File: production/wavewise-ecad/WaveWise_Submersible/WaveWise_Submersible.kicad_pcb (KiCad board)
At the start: 4 copper layers, 136.8 x 50.8 mm, 91 parts, among them J1 SMA_CONNECTOR, J10 Screw_Terminal_01x03, J11 Screw_Terminal_01x03, J2 SMA_CONNECTOR, J3 Screw_Terminal_01x04, J4 Screw_Terminal_01x03, J5 SMA_CONNECTOR, J6 USB_B_Micro, J7 Screw_Terminal_01x03, J8 Screw_Terminal_01x03, J9 Screw_Terminal_01x02, M1 MNMOS, M2 MNMOS, U1 ATMEGA328PB-ANR, U2 KP234XTMA1, U3 SI8600AC-B-ISR, U4 EZO_pH_Circuit, U5 SI8600AC-B-ISR, U6 EZO_Conductivity_Circuit, U7 TLV2462CP, U8 FT232RL-REEL, Y1 AS-16.000-20-SMD-TR

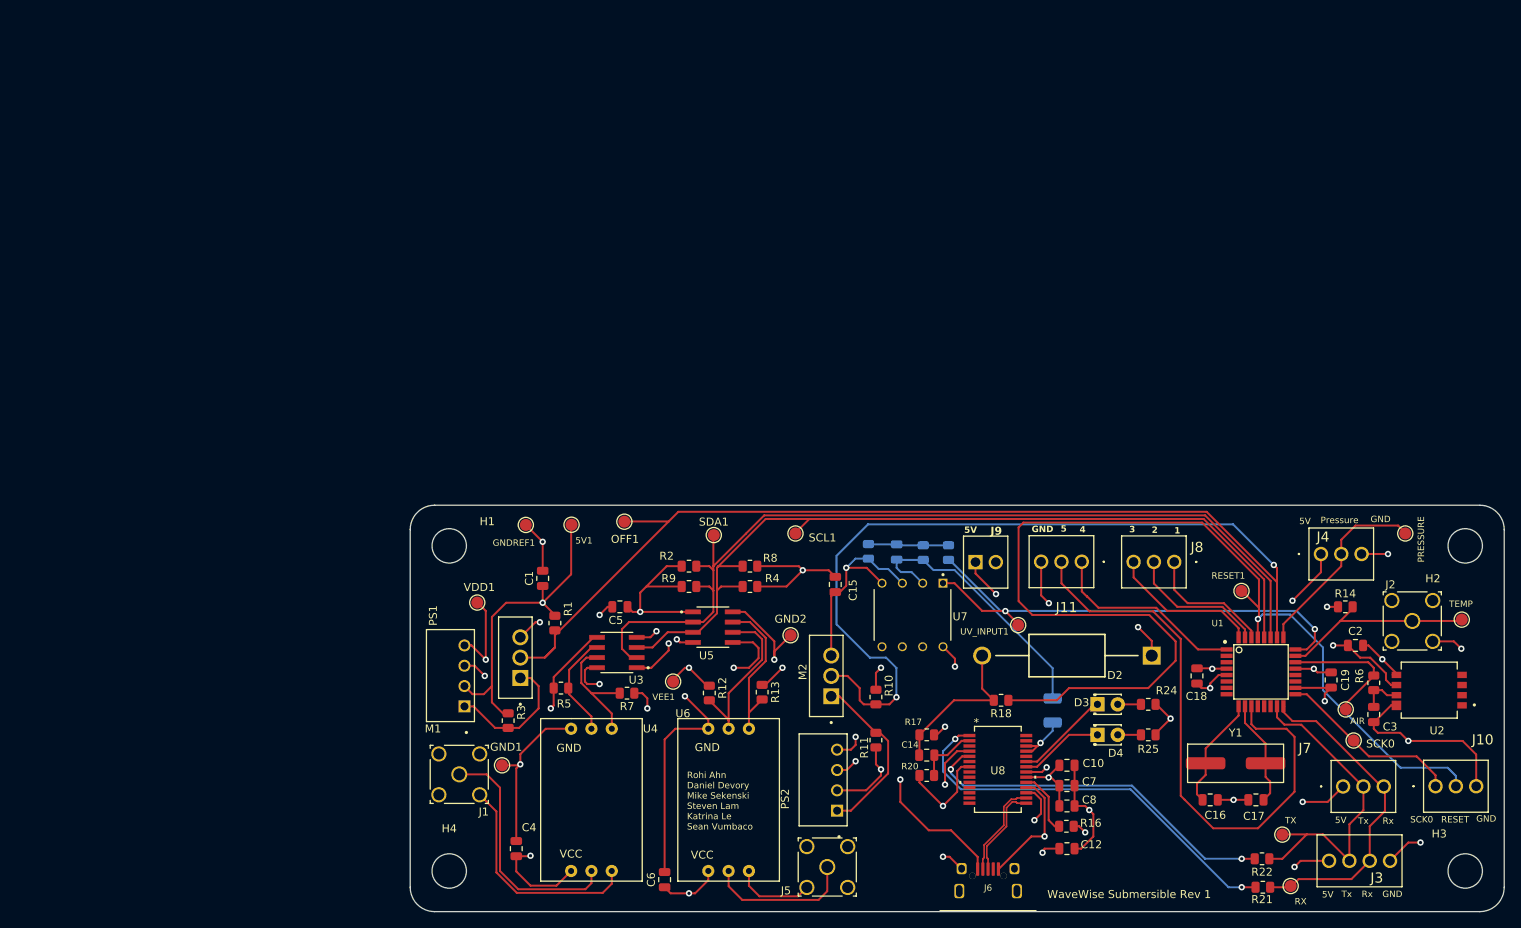
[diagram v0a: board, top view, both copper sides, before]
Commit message: layout first draft, added general/connector footprint
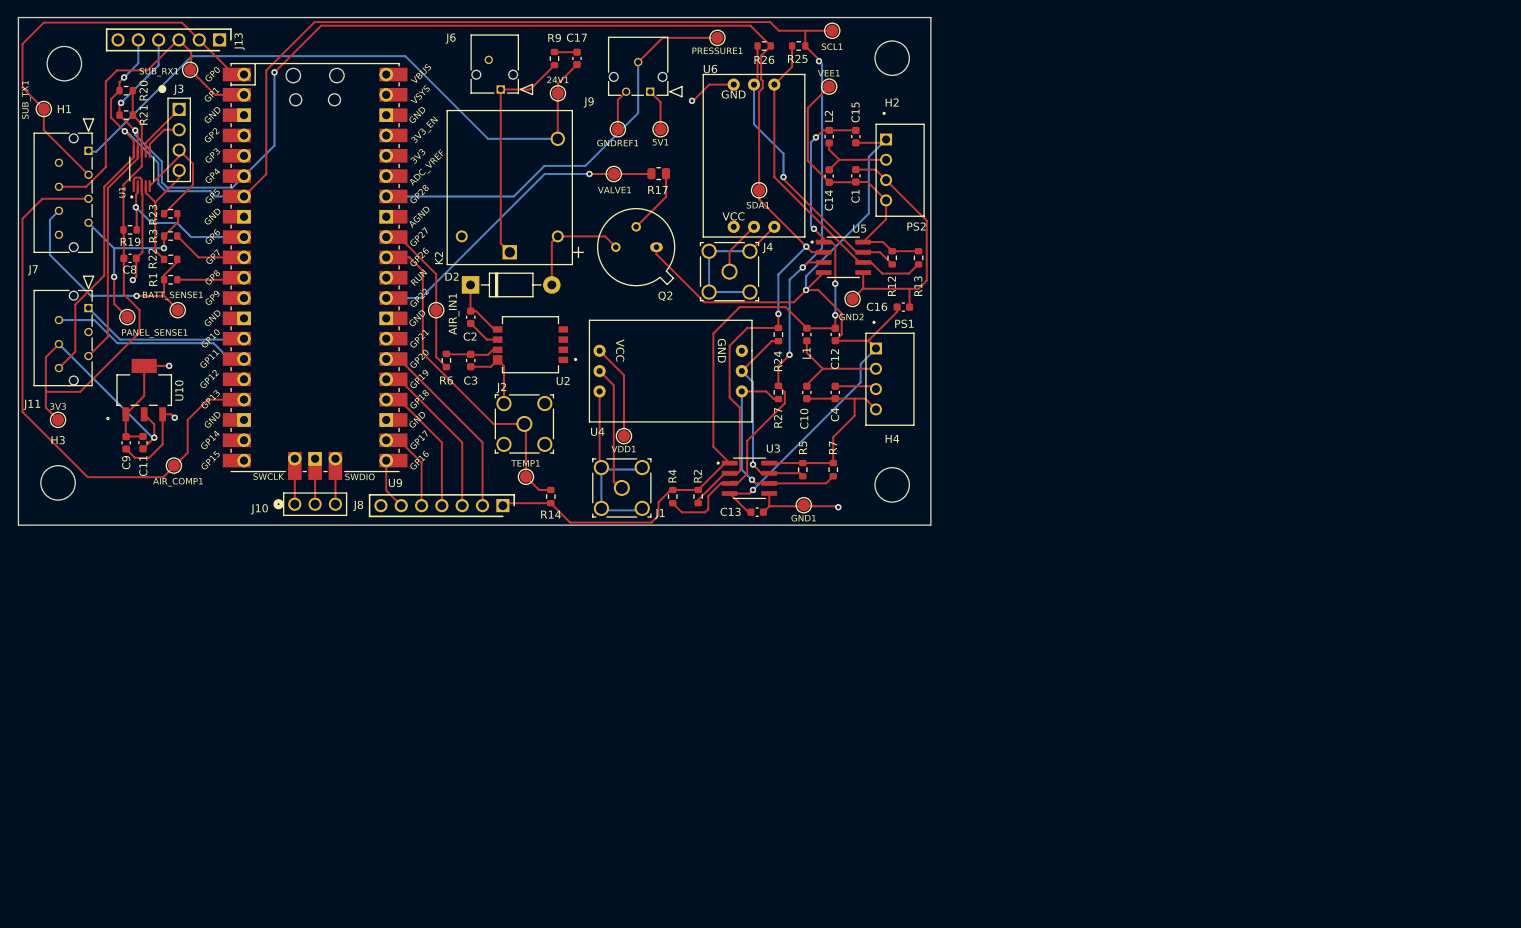
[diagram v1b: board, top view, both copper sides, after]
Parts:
- removed AIR, OFF1, PRESSURE, RESET1, RX, SCK0, TEMP, TX, UV_INPUT1: TestPoint, TestPoint:TestPoint_Pad_D1.5mm
- removed C18, C19, C7: 100n/10V, Capacitor_SMD:C_0805_2012Metric
- removed C5, C6: 1u/10V, Capacitor_SMD:C_0805_2012Metric
- removed D1: D_Photo, WW_Checked:GUVA-S12SD
- removed D3, D4: LED_S, LED_THT:LED_D1.8mm_W3.3mm_H2.4mm
- removed J5: SMA_CONNECTOR, Unchecked:SMA_Jack
- removed M1, M2: MNMOS, Unchecked:nMOS_ThroughHole
- removed R10, R11: 1M, Resistor_SMD:R_0805_2012Metric
- removed R15: 1k, Resistor_SMD:R_0805_2012Metric
- removed R16: 10k, Resistor_SMD:R_0805_2012Metric
- removed R18: 0, Resistor_SMD:R_0805_2012Metric
- removed R8: 10K, Resistor_SMD:R_0805_2012Metric
- removed U7: TLV2462CP, Unchecked:TLV2462CP
- removed U8: FT232RL-REEL, Unchecked:IC28_SSOP-28_FTD
- removed Y1: AS-16.000-20-SMD-TR, WW_Checked:WW_Oscillator
- added 24V1: TestPoint, TestPoint:TestPoint_Pad_D1.5mm, F.Cu at (105.0, 34.9)
- added 3V3: TestPoint, TestPoint:TestPoint_Pad_D1.5mm, F.Cu at (42.5, 75.7)
- added AIR_COMP1: TestPoint, TestPoint:TestPoint_Pad_D1.5mm, F.Cu at (57.0, 81.4)
- added AIR_IN1: TestPoint, TestPoint:TestPoint_Pad_D1.5mm, F.Cu at (89.8, 62.0)
- added BATT_SENSE1: TestPoint, TestPoint:TestPoint_Pad_D1.5mm, F.Cu at (57.5, 62.0)
- added C11: 22u, Capacitor_SMD:C_0603_1608Metric, F.Cu at (53.2, 78.5)
- added C9: 10u, Capacitor_SMD:C_0603_1608Metric, F.Cu at (51.1, 78.6)
- added J13: Conn_01x06_Pin, Connector:61300611121, F.Cu at (62.7, 28.2)
- added K2: AWHSH105D00G, Relay_SMD:AWHSH105D00G, F.Cu at (99.0, 54.8)
- added L1: 22u, Inductor_SMD:L_0603_1608Metric, F.Cu at (136.1, 65.0)
- added L2: 22u, Inductor_SMD:L_0603_1608Metric, F.Cu at (138.9, 40.3)
- added PANEL_SENSE1: TestPoint, TestPoint:TestPoint_Pad_D1.5mm, F.Cu at (51.2, 62.8)
- added PRESSURE1: TestPoint, TestPoint:TestPoint_Pad_D1.5mm, F.Cu at (125.0, 27.9)
- added Q2: 2N2219, Package_TO_SOT_THT:TO-39-3, F.Cu at (117.3, 54.1)
- added R26: 0, Resistor_SMD:R_0603_1608Metric, F.Cu at (130.8, 29.0)
- added R27: 0, Resistor_SMD:R_0603_1608Metric, F.Cu at (132.6, 72.3)
- added SUB_RX1: TestPoint, TestPoint:TestPoint_Pad_D1.5mm, F.Cu at (59.1, 31.9)
- added SUB_TX1: TestPoint, TestPoint:TestPoint_Pad_D1.5mm, F.Cu at (40.8, 36.8)
- added TEMP1: TestPoint, TestPoint:TestPoint_Pad_D1.5mm, F.Cu at (101.0, 82.8)
- added U10: AZ1117CH-3.3TRG1, Package_TO_SOT_SMD:SOT-223_DIO, F.Cu at (53.3, 72.0)
- added U9: Raspberry Pi Pico, MCU_RaspberryPi_and_Boards:RPi_Pico_SMD_TH, F.Cu at (74.7, 56.7)
- added VALVE1: TestPoint, TestPoint:TestPoint_Pad_D1.5mm, F.Cu at (112.0, 45.0)
- C1, C4: value 1u/10V -> 1u; footprint Capacitor_SMD:C_0805_2012Metric -> Capacitor_SMD:C_0603_1608Metric
- C10: value 4.7u/10V -> 330p; footprint Capacitor_SMD:C_0805_2012Metric -> Capacitor_SMD:C_0603_1608Metric
- C12: value 100n/10V -> 6.8u; footprint Capacitor_SMD:C_0805_2012Metric -> Capacitor_SMD:C_0603_1608Metric
- C13: value 0.1uF/10V -> 330p; footprint Capacitor_SMD:C_0805_2012Metric -> Capacitor_SMD:C_0603_1608Metric; moved to F.Cu
- C14: value 100n/10V -> 330p; footprint Capacitor_SMD:C_0805_2012Metric -> Capacitor_SMD:C_0603_1608Metric
- C15: value 0.1uF/10V -> 6.8u; footprint Capacitor_SMD:C_0805_2012Metric -> Capacitor_SMD:C_0603_1608Metric
- C16: value 22pF/10V -> 330p; footprint Capacitor_SMD:C_0805_2012Metric -> Capacitor_SMD:C_0603_1608Metric
- C17: value 22pF/10V -> 1u; footprint Capacitor_SMD:C_0805_2012Metric -> Capacitor_SMD:C_0603_1608Metric
- C2, C3: value 100nF/10V -> 100nF; footprint Capacitor_SMD:C_0805_2012Metric -> Capacitor_SMD:C_0603_1608Metric
- C8: value 100n/10V -> 0.1u; footprint Capacitor_SMD:C_0805_2012Metric -> Capacitor_SMD:C_0603_1608Metric
- D2: value 1N5822 -> 1N5817; footprint Unchecked:1N5822 -> Diode_THT:D_DO-41_SOD81_P10.16mm_Horizontal
- J1, J2: footprint Unchecked:SMA_Jack -> Connector:SMA_Jack
- J10: value Screw_Terminal_01x03 -> Conn_01x03_Pin; footprint WW_Checked:ScrewTerminal_01x03_2.54mm -> Connector:61300311121
- J11: value Screw_Terminal_01x03 -> 5031750600; footprint WW_Checked:ScrewTerminal_01x03_2.54mm -> Connector:5031750600
- J3: value Screw_Terminal_01x04 -> Conn_01x04_Pin; footprint WW_Checked:ScrewTerminal_01x04_2.54mm -> Connector:61300411121
- J4: value Screw_Terminal_01x03 -> SMA_CONNECTOR; footprint WW_Checked:ScrewTerminal_01x03_2.54mm -> Connector:SMA_Jack
- J6: value USB_B_Micro -> 5031750200; footprint WW_Checked:MicroUSB_Mount -> Connector:5031750200
- J7: value Screw_Terminal_01x03 -> 5031750800; footprint WW_Checked:ScrewTerminal_01x03_2.54mm -> Connector:5031750800
- J8: value Screw_Terminal_01x03 -> Conn_01x07_Pin; footprint WW_Checked:ScrewTerminal_01x03_2.54mm -> Connector:61300711121
- J9: value Screw_Terminal_01x02 -> 5031750300; footprint WW_Checked:ScrewTerminal_01x02_2.54mm -> Connector:5031750300
- PS1, PS2: footprint WW_Checked:RFM-0505S -> Converter_DCDC:RFM-0505S
- R1, R3: value 1M -> 0; footprint Resistor_SMD:R_0805_2012Metric -> Resistor_SMD:R_0603_1608Metric
- R12, R13, R14, R2, R4, R5, R6, R7: footprint Resistor_SMD:R_0805_2012Metric -> Resistor_SMD:R_0603_1608Metric
- R17: value 10k -> 5k
- R19: value 1M -> 10k; footprint Resistor_SMD:R_0805_2012Metric -> Resistor_SMD:R_0603_1608Metric; moved to F.Cu
- R20, R21: value 1k -> 10k; footprint Resistor_SMD:R_0805_2012Metric -> Resistor_SMD:R_0603_1608Metric
- R22: value 1k -> 0; footprint Resistor_SMD:R_0805_2012Metric -> Resistor_SMD:R_0603_1608Metric
- R23: value 3.3k -> 0; footprint Resistor_SMD:R_0805_2012Metric -> Resistor_SMD:R_0603_1608Metric; moved to F.Cu
- R24, R25: value R -> 0; footprint Resistor_SMD:R_0805_2012Metric -> Resistor_SMD:R_0603_1608Metric
- R9: value 10K -> 50; footprint Resistor_SMD:R_0805_2012Metric -> Resistor_SMD:R_0603_1608Metric
- U1: value ATMEGA328PB-ANR -> ADS1115IDGSR; footprint Unchecked:ATMEGA328PB-ANR -> Converter_ACDC:SOP50P490X110-10N
- U2: footprint Unchecked:XDCR_KP234XTMA1 -> Sensor_Pressure:XDCR_KP234XTMA1
- U3, U5: footprint Unchecked:SOIC127P600X175-8N -> Package_SO:SI8600AC-B-ISR
- U4: footprint WW_Checked:EZO_pH_Circuit -> Sensor:EZO_pH_Circuit
- U6: footprint WW_Checked:EZO_Conductivity_Circuit -> Sensor:EZO_Conductivity_Circuit
- moved H3 182.5 mm to (42.5, 83.6)
- moved J7 175.8 mm to (46.4, 42.1), turned to -90 degrees
- moved R21 171.8 mm to (51.1, 37.6), turned to 180 degrees
- moved J3 171.7 mm to (57.7, 36.9), turned to -90 degrees
- moved R22 155.6 mm to (56.6, 55.6), turned to 0 degrees
- moved U1 153.4 mm to (53.0, 44.3), turned to 90 degrees
- moved J10 146.9 mm to (72.1, 86.2)
- moved C8 135.6 mm to (51.5, 55.5), turned to 180 degrees
- moved R20 131.7 mm to (51.1, 34.5), turned to 180 degrees
- moved J11 128.1 mm to (46.4, 61.7), turned to -90 degrees
- moved C17 125.7 mm to (107.4, 30.5), turned to -90 degrees
- moved R6 122.7 mm to (91.1, 68.3), turned to -90 degrees
- moved C3 121.2 mm to (94.1, 68.3)
- moved U2 120.4 mm to (101.6, 66.3)
- moved C2 118.0 mm to (94.1, 62.9), turned to -90 degrees
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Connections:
- C1 pad 1: +5V -> VEE
- C1 pad 2: GNDREF -> GND2
- C10 pad 1: +5V -> VDD
- C10 pad 2: GNDREF -> Net-(PS1-+VIN)
- C12 pad 1: +3V3 -> +5V
- C13 pad 1: Net-(D1-K) -> GND1
- C13 pad 2: Net-(C13-Pad2) -> GNDREF
- C14 pad 1: Net-(C14-Pad1) -> VEE
- C14 pad 2: Net-(U8-DTR#) -> Net-(PS2-+VIN)
- C16 pad 1: Net-(U1-PD5) -> GND2
- C17 pad 1: Net-(U1-PD6) -> Net-(C17-Pad1)
- C17 pad 2: GNDREF -> +24V
- C8 pad 1: +5V -> GNDREF
- C8 pad 2: GNDREF -> +3V3
- J1 pad 2: (no net) -> Net-(U4-PGND)
- J1 pad 3: (no net) -> Net-(U4-PGND)
- J1 pad 5: (no net) -> Net-(U4-PGND)
- J10 pad 1: SCK0 -> SWCLK
- J10 pad 2: RESET -> GND
- J10 pad 3: GNDREF -> SWDIO
- J11 pad 1: EXTGPIO4 -> SYNC
- J11 pad 2: EXTGPIO5 -> READY/INT
- J2 pad 2: (no net) -> GNDREF
- J2 pad 3: (no net) -> GNDREF
- J2 pad 5: (no net) -> GNDREF
- J3 pad 1: +5V -> /ADC3
- J3 pad 2: SUB_TX -> /ADC2
- J3 pad 3: SUB_RX -> /ADC1
- J3 pad 4: GNDREF -> /ADC0
- J4 pad 1: +5V -> Net-(U6-PRB)
- J4 pad 2: PRESSURE_INPUT -> Net-(U6-PGND)
- J4 pad 3: GNDREF -> Net-(U6-PGND)
- J6 pad 1: +5V -> Net-(J6-Pad1)
- J6 pad 2: /USB- -> GNDREF
- J7 pad 1: +5V -> +24V
- J7 pad 2: SUB_TX -> +5V
- J7 pad 3: SUB_RX -> SUB_TX
- J8 pad 1: EXTGPIO1 -> +5V
- J8 pad 2: EXTGPIO2 -> EXTGPIO1
- J8 pad 3: EXTGPIO3 -> EXTGPIO2
- J9 pad 2: unconnected-(J9-Pin_2-Pad2) -> PRESSURE_INPUT
- PS1 pad 1: Net-(M1-D) -> GNDREF
- PS1 pad 2: +5V -> Net-(PS1-+VIN)
- PS2 pad 1: Net-(M2-D) -> GNDREF
- PS2 pad 2: +5V -> Net-(PS2-+VIN)
- R1 pad 1: +5V -> BATTERY_SENSE
- R1 pad 2: OFF -> Net-(U9-GPIO8)
- R17 pad 1: Net-(C14-Pad1) -> VALVE_OUT
- R17 pad 2: +5V -> Net-(Q2-B)
- R19 pad 1: Net-(D1-K) -> +3V3
- R19 pad 2: Net-(C13-Pad2) -> ADC_RDY
- R20 pad 1: GNDREF -> +3V3
- R20 pad 2: Net-(U8-DTR#) -> SCL
- R21 pad 1: Net-(U8-TXD) -> +3V3
- R21 pad 2: SUB_RX -> SDA
- R22 pad 1: SUB_TX -> /ADC0
- R22 pad 2: Net-(U8-RXD) -> BATTERY_SENSE
- R23 pad 1: UV_INPUT -> /ADC1
- R23 pad 2: Net-(C13-Pad2) -> PANEL_SENSE
- R24 pad 1: Net-(D3-A) -> SDA
- R24 pad 2: +5V -> Net-(U3-BSDA)
- R25 pad 1: Net-(D4-A) -> SCL
- R25 pad 2: +5V -> Net-(U5-BSCL)
- R3 pad 1: +5V -> PANEL_SENSE
- R3 pad 2: Net-(M1-D) -> Net-(U9-GPIO7)
- R6 pad 2: AIROUT -> AIR_INPUT
- R9 pad 1: +5V -> Net-(C17-Pad1)
- R9 pad 2: SDA -> Net-(J6-Pad1)
- U1 pad 1: EXTGPIO4 -> GNDREF
- U1 pad 10: Net-(U1-PD6) -> SCL
- U1 pad 2: unconnected-(U1-PD4-Pad2) -> ADC_RDY
- U1 pad 3: unconnected-(U1-PE0-Pad3) -> GNDREF
- U1 pad 4: +5V -> /ADC0
- U1 pad 5: GNDREF -> /ADC1
- U1 pad 6: unconnected-(U1-PE1-Pad6) -> /ADC2
- U1 pad 7: unconnected-(U1-PB6-Pad7) -> /ADC3
- U1 pad 8: unconnected-(U1-PB7-Pad8) -> +3V3
- U1 pad 9: Net-(U1-PD5) -> SDA
- U3 pad 5: VDD -> GND1
- U3 pad 6: Net-(U3-BSDA) -> Net-(U3-BSCL)
- U3 pad 7: Net-(U3-BSCL) -> Net-(U3-BSDA)
- U3 pad 8: GND1 -> VDD
- U5 pad 5: VEE -> GND2
- U5 pad 6: Net-(U5-BSDA) -> Net-(U5-BSCL)
- U5 pad 7: Net-(U5-BSCL) -> Net-(U5-BSDA)
- U5 pad 8: GND2 -> VEE
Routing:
- net OFF: track 214.5 -> 0.00 mm, vias 2 -> 0
- net RESET: track 137.8 -> 0.00 mm, vias 1 -> 0
- net SCL: track 108.1 -> 235.8 mm, vias 0 -> 5
- net SDA: track 114.7 -> 216.6 mm, vias 0 -> 5
- net +24V: track 0.00 -> 78.2 mm
- net +3V3: track 7.78 -> 80.2 mm, vias 2 -> 1
- net AIR_COMP: track 0.00 -> 70.9 mm
- net EXTGPIO5: track 73.1 -> 6.41 mm
- net UV_INPUT: track 65.4 -> 0.00 mm, vias 2 -> 0
- net +5V: track 188.3 -> 123.5 mm, vias 22 -> 5
- net Net-(U8-TXD): track 51.7 -> 0.00 mm, vias 2 -> 0
- net Net-(U8-RXD): track 46.0 -> 0.00 mm, vias 2 -> 0
- net VALVE_OUT: track 0.00 -> 39.6 mm, vias 0 -> 1
- net Net-(D1-K): track 34.0 -> 0.00 mm
- net BATTERY_SENSE: track 0.00 -> 30.1 mm, vias 0 -> 1
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- added copper zone on In1.Cu, net +5V
- added copper zone on In2.Cu, net GND1
- added copper zone on In2.Cu, net GND2
- added copper zone on In2.Cu, net GNDREF
- added copper zone on In1.Cu, net VDD
- added copper zone on In1.Cu, net VEE
- removed copper zone on In2.Cu, net +3V3
- removed copper zone on In2.Cu, net +5V
- removed copper zone on In1.Cu, net GND1
- removed copper zone on In1.Cu, net GND2
- removed copper zone on In1.Cu, net GNDREF
- removed copper zone on In2.Cu, net VDD
- removed copper zone on In2.Cu, net VEE
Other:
- board size 136.8 x 50.8 mm -> 114 x 63.4 mm
- board text removed: "1"
- board text removed: "2"
- board text removed: "3"
- board text removed: "4"
- board text removed: "5"
- board text removed: "5V"
- board text removed: "GND"
- board text removed: "Pressure"
- board text removed: "RESET"
- board text removed: "Rohi Ahn Daniel Devory Mike Sekenski Steven Lam Katrina Le Sean Vumbaco"
- board text removed: "Rx"
- board text removed: "SCK0"
- board text removed: "Tx"
- board text removed: "WaveWise Submersible Rev 1"

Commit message: Sub layout draft 2 for chiefs
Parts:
- added G***: LOGO, LOGO, F.Cu at (78.5, 45.1)
- added G***: LOGO, LOGO, F.Cu at (74.6, 68.7)
- added G***: LOGO, LOGO, B.Cu at (74.4, 56.4)
- added R10: 0, Resistor_SMD:R_0603_1608Metric, F.Cu at (146.8, 35.6)
- added R11: 0, Resistor_SMD:R_0603_1608Metric, F.Cu at (146.3, 79.2)
- added R15: 0, Resistor_SMD:R_0603_1608Metric, F.Cu at (48.5, 83.8)
- added R8: 0, Resistor_SMD:R_0603_1608Metric, F.Cu at (42.8, 35.7)
- H1, H2, H3, H4: footprint MountingHole:MountingHole_4.3mm_M4 -> MountingHole:MountingHole_3.2mm_M3_DIN965_Pad
- moved SDA1 53.3 mm to (80.4, 27.9)
- moved SUB_TX1 29.2 mm to (68.6, 27.9)
- moved R2 3.72 mm to (121.3, 81.8), turned to 0 degrees
- moved 3V3 2.97 mm to (45.3, 76.7)
- moved R4 2.03 mm to (121.3, 84.6), turned to 0 degrees
- moved PS1 1.30 mm to (147.8, 70.9)
- moved H1 1.14 mm to (42.4, 30.5)
- moved H3 0.28 mm to (42.4, 83.8)
- moved H2 0.25 mm to (146.6, 30.5)
- moved H4 0.25 mm to (146.6, 83.8)
- moved J4 0.24 mm to (126.5, 57.4)
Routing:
- net GNDREF: track 154.0 -> 190.1 mm, vias 4 -> 6
- net SUB_TX: track 51.2 -> 37.9 mm
- net Net-(H1-Pad1): track 0.00 -> 6.29 mm
- net Net-(H3-Pad1): track 0.00 -> 5.27 mm
- net Net-(H4-Pad1): track 0.00 -> 4.81 mm
- net Net-(H2-Pad1): track 0.00 -> 4.36 mm
- net SCL: track 235.8 -> 231.5 mm
- net AIR_COMP: track 70.9 -> 67.3 mm
- net GND2: track 39.7 -> 36.5 mm, vias 1 -> 2
- net +5V: track 123.5 -> 126.8 mm, vias 5 -> 7
- net +3V3: track 80.2 -> 83.4 mm
- net SDA: track 216.6 -> 214.4 mm
- net VDD: track 38.3 -> 39.7 mm
- net Net-(PS1-+VIN): track 14.0 -> 15.3 mm
- net GND1: track 16.5 -> 17.9 mm
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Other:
- board size 114 x 63.4 mm -> 114.3 x 63.5 mm
- board text added: "5V"
- board text added: "ADC0"
- board text added: "ADC1"
- board text added: "ADC2"
- board text added: "ADC3"
- board text added: "Buoy Comms"
- board text added: "Conductivity"
- board text added: "GND"
- board text added: "GPIO1"
- board text added: "GPIO2"
- board text added: "GPIO3"
- board text added: "GPIO4"
- board text added: "GPIO5"
- board text added: "RX"
- board text added: "SCL"
- board text added: "SDA"
- board text added: "Sub Board WaveWise Sam Moy Katie Dewhurst Billy Ferros Sophia Wang"
- board text added: "TX"
- board text added: "Temp"
- board text added: "UV"
- board text added: "Valve"
- board text added: "Water Pressure"
- board text added: "pH"

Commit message: Sub pcb draft 3
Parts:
- removed C8: 0.1u, Capacitor_SMD:C_0603_1608Metric
- added C5: 0.1u, Capacitor_SMD:C_0805_2012Metric, F.Cu at (51.9, 40.1)
- added C6: 0.1u, Capacitor_SMD:C_0805_2012Metric, F.Cu at (54.4, 40.1)
- C1, C10, C11, C12, C13, C14, C15, C16, C17, C2, C3, C4, C9: footprint Capacitor_SMD:C_0603_1608Metric -> Capacitor_SMD:C_0805_2012Metric
- H1, H2, H3, H4: footprint MountingHole:MountingHole_3.2mm_M3_DIN965_Pad -> MountingHole:MountingHole_3.2mm_M3_ISO7380_Pad
- J11: value 5031750600 -> 55935-0610; footprint Connector:5031750600 -> Connector_Molex:Molex_MicroClasp_55935-0610_1x06_P2.00mm_Horizontal
- J6: value 5031750200 -> 55932-0210; footprint Connector:5031750200 -> Connector_Molex:Molex_MicroClasp_55932-0210_1x02_P2.00mm_Vertical
- J7: value 5031750800 -> 55935-0810; footprint Connector:5031750800 -> Connector_Molex:Molex_MicroClasp_55935-0810_1x08_P2.00mm_Horizontal
- J9: value 5031750300 -> 55932-0310; footprint Connector:5031750300 -> Connector_Molex:Molex_MicroClasp_55932-0310_1x03_P2.00mm_Vertical
- L1, L2: footprint Inductor_SMD:L_0603_1608Metric -> Inductor_SMD:SRP6060FA220M
- R1, R10, R11, R12, R13, R14, R15, R19, R2, R20, R21, R22, R23, R24, R25, R26, R27, R3, R4, R5, R6, R7, R8, R9: footprint Resistor_SMD:R_0603_1608Metric -> Resistor_SMD:R_0805_2012Metric
- moved SCL1 51.4 mm to (87.9, 27.0)
- moved C12 18.8 mm to (126.1, 78.0), turned to 90 degrees
- moved C15 14.4 mm to (134.4, 52.4), turned to 90 degrees
- moved VEE1 10.7 mm to (135.8, 44.2)
- moved C11 10.4 mm to (57.2, 69.0)
- moved C4 9.71 mm to (131.4, 77.3)
- moved C9 9.62 mm to (52.7, 69.1)
- moved 5V1 7.46 mm to (111.0, 36.4)
- moved 3V3 7.07 mm to (51.5, 80.2), turned to 90 degrees
- moved J9 6.40 mm to (112.2, 30.0), turned to 0 degrees
- moved L1 6.25 mm to (139.0, 70.6), turned to 0 degrees
- moved GND1 6.05 mm to (141.8, 85.8)
- moved R19 5.65 mm to (54.6, 56.7), turned to 90 degrees
- moved GNDREF1 5.41 mm to (117.1, 36.5)
- moved C1 5.20 mm to (142.9, 50.3)
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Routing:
- net +3V3: track 83.4 -> 67.9 mm, vias 1 -> 0
- net VDD: track 39.7 -> 26.9 mm, vias 0 -> 1
- net +5V: track 126.8 -> 137.8 mm, vias 7 -> 8
- net GNDREF: track 190.1 -> 180.9 mm, vias 6 -> 15
- net SDA: track 214.4 -> 223.5 mm
- net VEE: track 36.0 -> 27.3 mm
- net READY/INT: track 25.1 -> 18.3 mm
- net GND2: track 36.5 -> 30.3 mm, vias 2 -> 3
- net Net-(PS2-+VIN): track 10.3 -> 13.9 mm
- net SCL: track 231.5 -> 235.2 mm
- net Net-(J6-Pad1): track 28.8 -> 31.9 mm
- net SYNC: track 21.0 -> 18.1 mm
- net Net-(U3-BSCL): track 27.0 -> 24.3 mm
- net BATTERY_SENSE: track 30.1 -> 27.4 mm
- net Net-(C5-Pad1): track 0.00 -> 2.55 mm
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
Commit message: change sub vias to through and create step file for pmic
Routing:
- net GNDREF: track 180.9 -> 176.5 mm
- net GND1: track 17.5 -> 18.6 mm
